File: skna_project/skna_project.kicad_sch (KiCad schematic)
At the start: 23 parts, among them J2 SWD, SW1 SW_SPDT, U1 STM32F405RGT6, Y1 16MHz

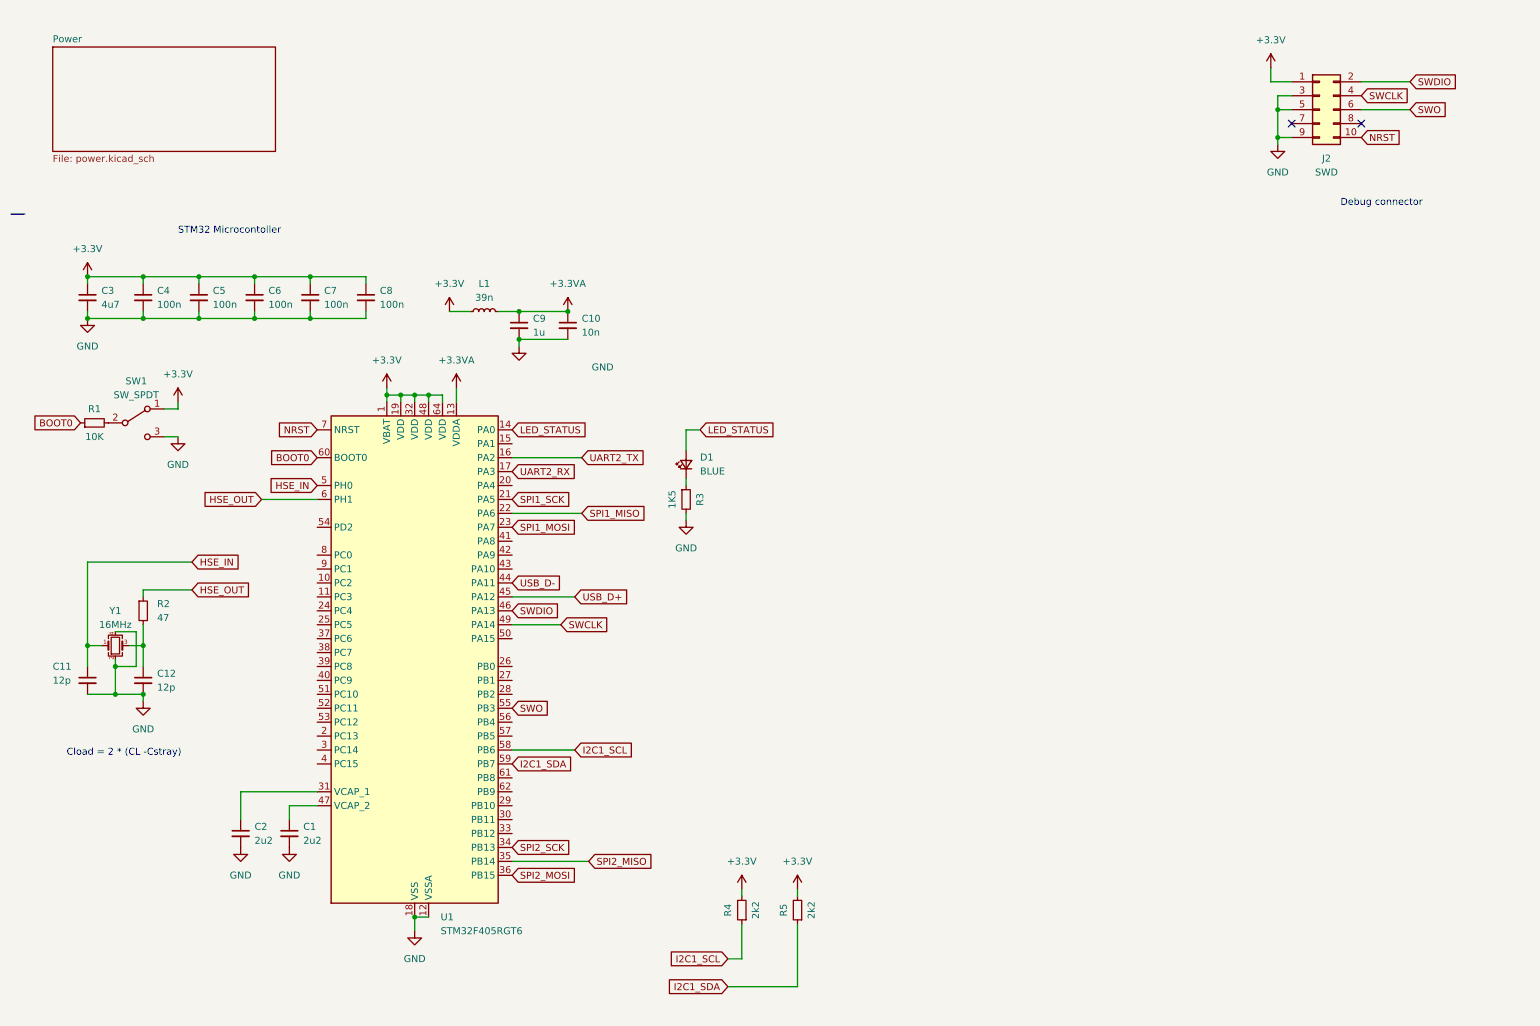
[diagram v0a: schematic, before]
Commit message: added flash drive to circuit
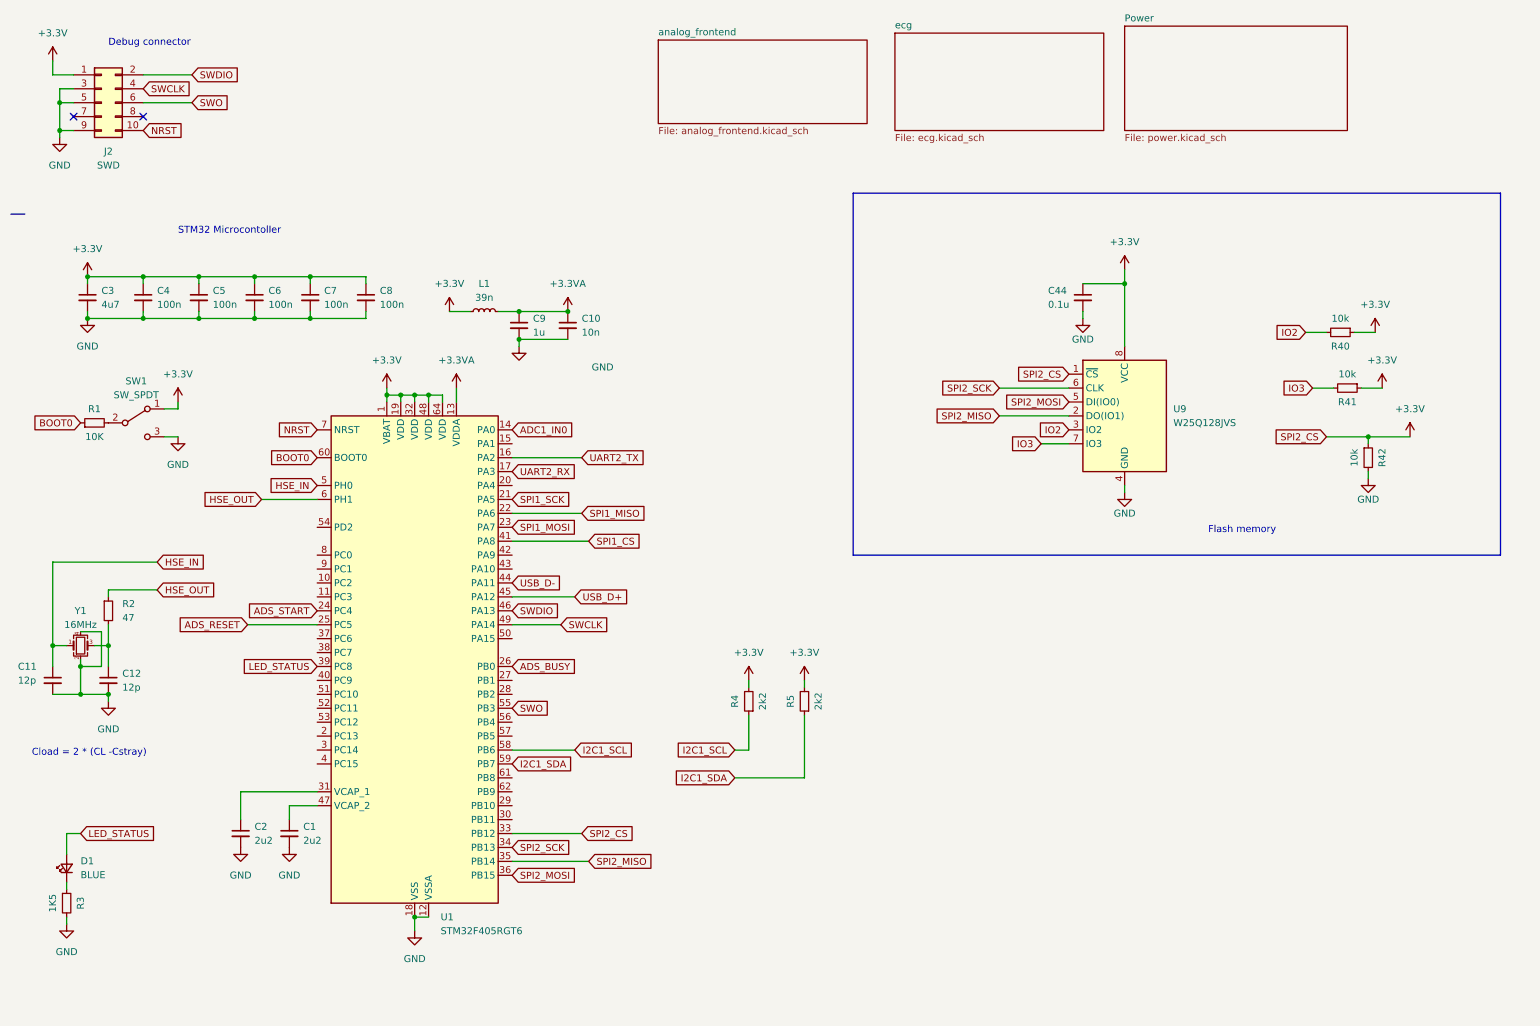
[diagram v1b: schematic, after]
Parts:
- added C44: 0.1u, symbol Device:C_Small
- added R40, R41, R42: 10k, symbol Device:R_Small
- added U9: W25Q128JVS, Package_SO:SOIC-8_5.23x5.23mm_P1.27mm, symbol Memory_Flash:W25Q128JVS
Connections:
- net +3.3V: now also U1.33 (PB12), C44.1, R40.1, R41.1, R42.1, U9.1 (~{CS}), U9.8 (VCC)
- net GND: now also C44.2, R42.2, U9.4 (GND)
- net LED_STATUS: now also U1.39 (PC8); no longer U1.14 (PA0)
- net SPI2_MISO: now also U9.2 (DO(IO1))
- net SPI2_MOSI: now also U9.5 (DI(IO0))
- net SPI2_SCK: now also U9.6 (CLK)
- net ADS_START: now reaches U1.24 (PC4)
- net ADS_RESET: now reaches U1.25 (PC5)
- net ADS_BUSY: now reaches U1.26 (PB0)
- net SPI1_CS: now reaches U1.41 (PA8)
- new net ADC1_IN0: U1.14 (PA0)
- new net IO2: R40.2, U9.3 (IO2)
- new net IO3: R41.2, U9.7 (IO3)
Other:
- added sheet analog_frontend (analog_frontend.kicad_sch)
- added sheet ecg (ecg.kicad_sch)
- note added: "Flash memory"
- moved on the sheet: C11, C12, D1, J2, R2, R3, R4, R5, Y1

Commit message: Replaced ADS129 with ADS8232
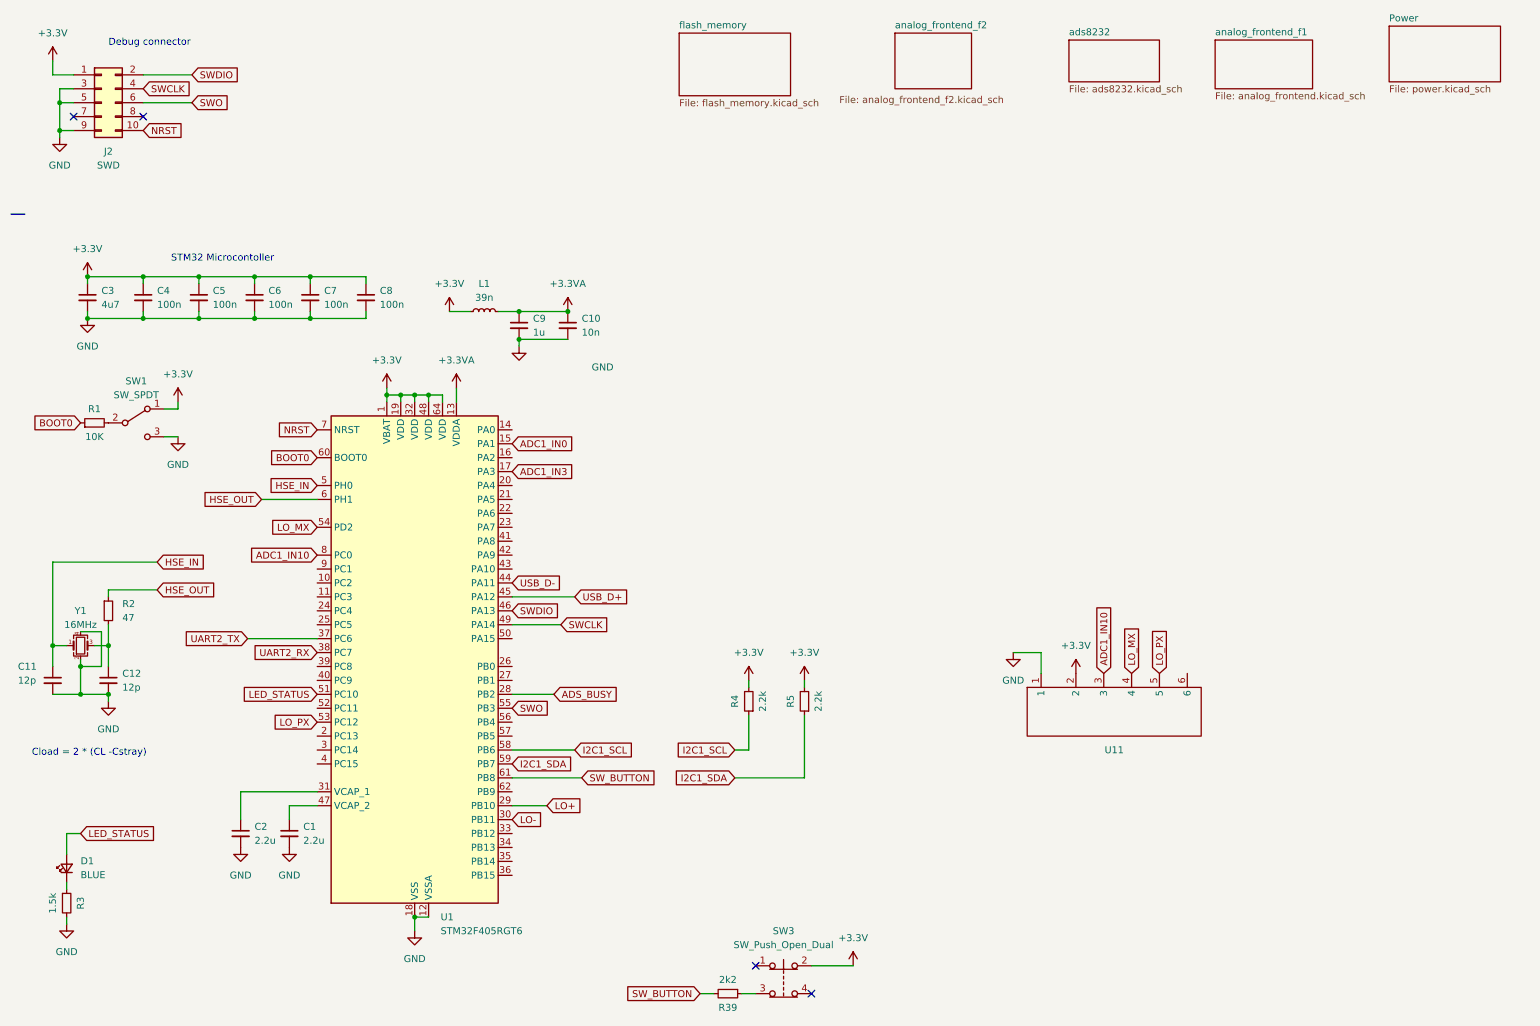
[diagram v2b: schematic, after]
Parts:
- removed C44: 0.1u, symbol Device:C_Small
- removed R40, R41, R42: 10k, symbol Device:R_Small
- removed U9: W25Q128JVS, Package_SO:SOIC-8_5.23x5.23mm_P1.27mm, symbol Memory_Flash:W25Q128JVS
- added R39: 2k2, symbol Device:R_Small
- added SW3: SW_Push_Open_Dual, symbol Switch:SW_Push_Open_Dual
- added U11: ~, symbol custom_regulator:header
- C1, C2: value 2u2 -> 2.2u
- R3: value 1K5 -> 1.5k
- R4, R5: value 2k2 -> 2.2k
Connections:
- net +3.3V: now also SW3.2, U11.2; no longer U1.33 (PB12)
- net ADC1_IN0: now also U1.15 (PA1); no longer U1.14 (PA0)
- net ADS_BUSY: now also U1.28 (PB2); no longer U1.26 (PB0)
- net GND: now also U11.1
- net LED_STATUS: now also U1.51 (PC10); no longer U1.39 (PC8)
- net UART2_RX: now also U1.38 (PC7); no longer U1.17 (PA3)
- net UART2_TX: now also U1.37 (PC6); no longer U1.16 (PA2)
- net LO+: now reaches U1.29 (PB10)
- net LO-: now reaches U1.30 (PB11)
- net LO_PX: now reaches U1.53 (PC12)
- net LO_PX: now also U11.5
- net LO_MX: now reaches U1.54 (PD2)
- net LO_MX: now also U11.4
- net SW_BUTTON: now reaches U1.61 (PB8)
- net SW_BUTTON: now also R39.2
- net ADC1_IN10: now reaches U1.8 (PC0)
- net ADC1_IN10: now also U11.3
- net ADS_RESET: no longer names the net of U1.25 (PC5)
- net ADS_START: no longer names the net of U1.24 (PC4)
- net SPI1_CS: no longer names the net of U1.41 (PA8)
- net SPI1_MISO: no longer names the net of U1.22 (PA6)
- net SPI1_MOSI: no longer names the net of U1.23 (PA7)
- net SPI1_SCK: no longer names the net of U1.21 (PA5)
- net SPI2_MISO: no longer names the net of U1.35 (PB14)
- net SPI2_MOSI: no longer names the net of U1.36 (PB15)
- net SPI2_SCK: no longer names the net of U1.34 (PB13)
- new net: R39.1, SW3.3
- new net ADC1_IN3: U1.17 (PA3)
- no-connect marks 2 -> 4
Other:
- sheet analog_frontend renamed analog_frontend_f1
- removed sheet ecg
- added sheet ads8232 (ads8232.kicad_sch)
- added sheet analog_frontend_f2 (analog_frontend_f2.kicad_sch)
- added sheet flash_memory (flash_memory.kicad_sch)
- note removed: "Flash memory"
